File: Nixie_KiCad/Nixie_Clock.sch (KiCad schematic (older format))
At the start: 18 parts, among them U1 K155ID1, U10 K155ID1, U11 IN-14, U12 DS3231, U2 IN-14, U3 K155ID1, U4 IN-14, U5 K155ID1, U6 IN-3, U7 PS_V2H, U8 K155ID1, U9 IN-14

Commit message: Added PCB
-Added PCB ratsnest
-Added Netlist
-Changed Arduino module
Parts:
- removed A1: Arduino_UNO_R3, Module:Arduino_UNO_R3, symbol Nixie_Lib:Arduino_UNO_R3
- added A1: Arduino_Nano_Every, Module:Arduino_Nano, symbol Nixie_Lib:Arduino_Nano_Every
- added R4, R5, R6: 10k, Resistor_THT:R_Axial_DIN0207_L6.3mm_D2.5mm_P7.62mm_Horizontal, symbol Device:R
- added R7: 5k1, Resistor_THT:R_Axial_DIN0207_L6.3mm_D2.5mm_P7.62mm_Horizontal, symbol Device:R
- R1, R2: footprint (none) -> Resistor_THT:R_Axial_DIN0207_L6.3mm_D2.5mm_P7.62mm_Horizontal
- R3: value 137.5k -> 100k; footprint (none) -> Resistor_THT:R_Axial_DIN0207_L6.3mm_D2.5mm_P7.62mm_Horizontal
- R8: renamed from R4; footprint (none) -> Resistor_THT:R_Axial_DIN0207_L6.3mm_D2.5mm_P7.62mm_Horizontal
- R9: renamed from R5; footprint (none) -> Resistor_THT:R_Axial_DIN0207_L6.3mm_D2.5mm_P7.62mm_Horizontal
- U1, U10, U3, U5, U8: footprint (none) -> Nixie_Clock_Footprint:K155ID1
- U11, U2, U4, U9: footprint (none) -> Nixie_Clock_Footprint:IN-14
- U12: footprint (none) -> Nixie_Clock_Footprint:DS3231
- U6: footprint (none) -> Nixie_Clock_Footprint:IN-3
- U7: footprint (none) -> Nixie_Clock_Footprint:PS_V2H
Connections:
- wire segments 134 -> 146
- no-connect marks 29 -> 27
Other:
- note added: "Can add switch to cathode here to\npermanently turn on DEC"
- moved on the sheet: R3

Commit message: Finalized Design
- Finalized PCB design
- Generated Gerber files
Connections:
- net GND: no longer U12.6 (GND)
- net at A1.29 (GND), A1.4 (GND): now also U12.6 (GND)
- no-connect marks 27 -> 26
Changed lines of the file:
@@
 Wire Wire Line
 	6950 4500 6950 4400
-$Comp
-L power:GND #PWR021
-U 1 1 61CE0EAF
-P 6950 4700
-F 0 "#PWR021" H 6950 4450 50  0001 C CNN
-F 1 "GND" H 6955 4527 50  0000 C CNN
-F 2 "" H 6950 4700 50  0001 C CNN
-F 3 "" H 6950 4700 50  0001 C CNN
-	1    6950 4700
-	1    0    0    -1
-$EndComp
 Wire Wire Line
 	6950 4700 6950 4600
@@
 NoConn ~ 7650 2550
 $Comp
-L power:GND #PWR023
-U 1 1 61D94328
-P 1600 5450
-F 0 "#PWR023" H 1600 5200 50  0001 C CNN
-F 1 "GND" H 1605 5277 50  0000 C CNN
-F 2 "" H 1600 5450 50  0001 C CNN
-F 3 "" H 1600 5450 50  0001 C CNN
-	1    1600 5450
-	1    0    0    -1
-$EndComp
-$Comp
 L Nixie_Lib:IN-3 U6
 U 1 1 61DA4CEC
@@
 $EndComp
 Wire Wire Line
-	1600 5350 1600 5450
-Wire Wire Line
 	1600 4650 1500 4650
 $Comp
@@
 NoConn ~ 1200 3650
 NoConn ~ 1600 4050
-NoConn ~ 1700 2050
 $Comp
 L Nixie_Lib:Arduino_Nano_Every A1
@@
 	-1   0    0    1
 $EndComp
+Wire Wire Line
+	1600 5350 2550 5350
+Wire Wire Line
+	2550 5350 2550 2050
+Wire Wire Line
+	2550 2050 1700 2050
+$Comp
+L power:Earth #PWR?
+U 1 1 61D64376
+P 6950 4700
+F 0 "#PWR?" H 6950 4450 50  0001 C CNN
+F 1 "Earth" H 6950 4550 50  0001 C CNN
+F 2 "" H 6950 4700 50  0001 C CNN
+F 3 "~" H 6950 4700 50  0001 C CNN
+	1    6950 4700
+	1    0    0    -1
+$EndComp
 $EndSCHEMATC

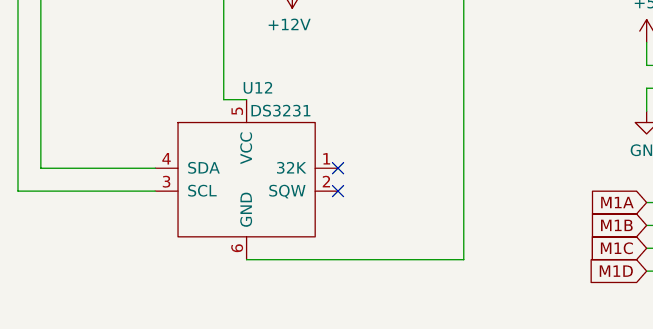
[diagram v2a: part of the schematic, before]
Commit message: Added Drill Holes
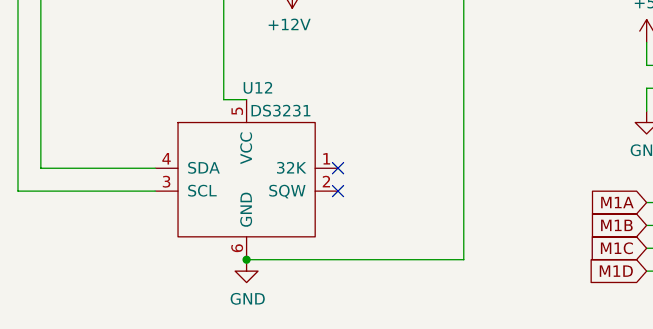
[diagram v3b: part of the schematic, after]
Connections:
- net GND: now also A1.29 (GND), A1.4 (GND), U12.6 (GND)
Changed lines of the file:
@@
 	1    0    0    -1
 $EndComp
+$Comp
+L power:GND #PWR?
+U 1 1 61CE4D4F
+P 1600 5350
+F 0 "#PWR?" H 1600 5100 50  0001 C CNN
+F 1 "GND" H 1605 5177 50  0000 C CNN
+F 2 "" H 1600 5350 50  0001 C CNN
+F 3 "" H 1600 5350 50  0001 C CNN
+	1    1600 5350
+	1    0    0    -1
+$EndComp
+Connection ~ 1600 5350
 $EndSCHEMATC

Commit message: minor updates
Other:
- note added: "Can add optional 100nF\nfilter capacitor here\nand/or voltage rectifier"
- note removed: "Can add optional 100nF\nfilter capacitor here"
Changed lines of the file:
@@
 $EndComp
 Text Notes 8400 4500 0    50   ~ 0
-Can add optional 100nF\nfilter capacitor here
+Can add optional 100nF\nfilter capacitor here\nand/or voltage rectifier
 $Comp
 L Nixie_Lib:DS3231 U12

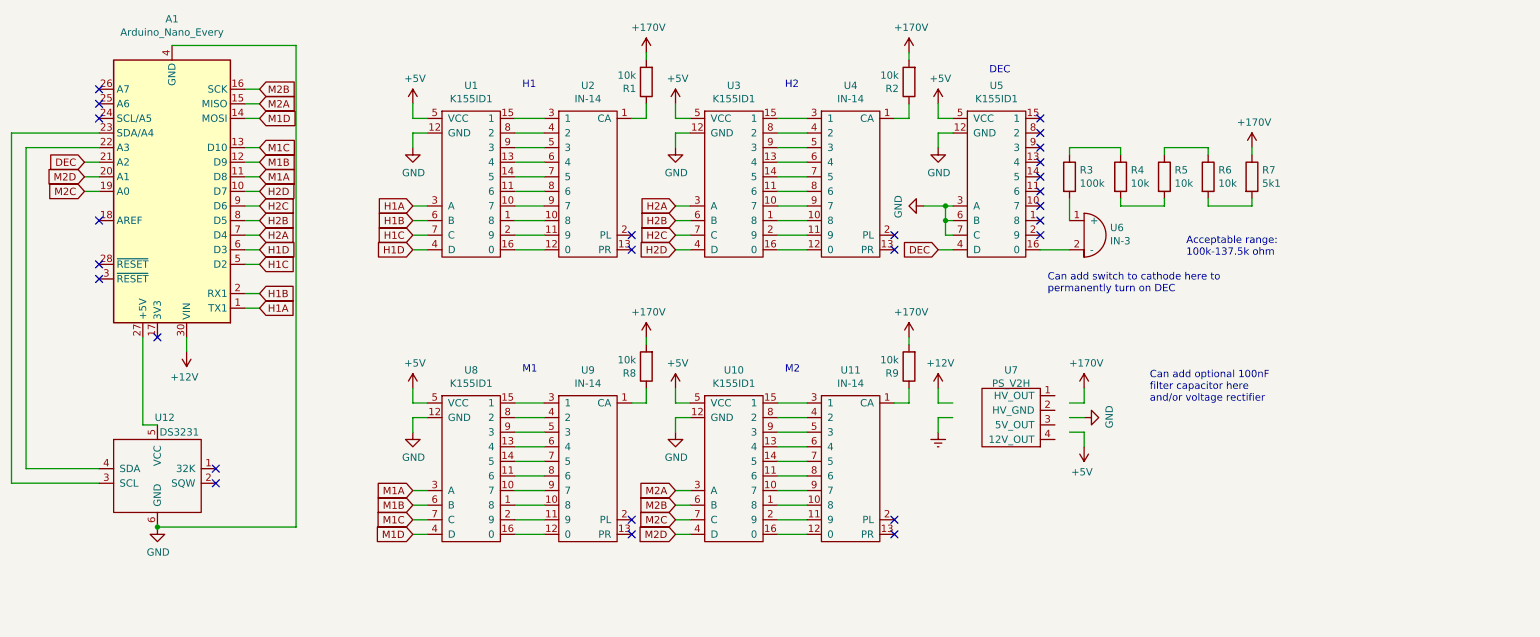
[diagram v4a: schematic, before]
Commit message: added filter capacitors
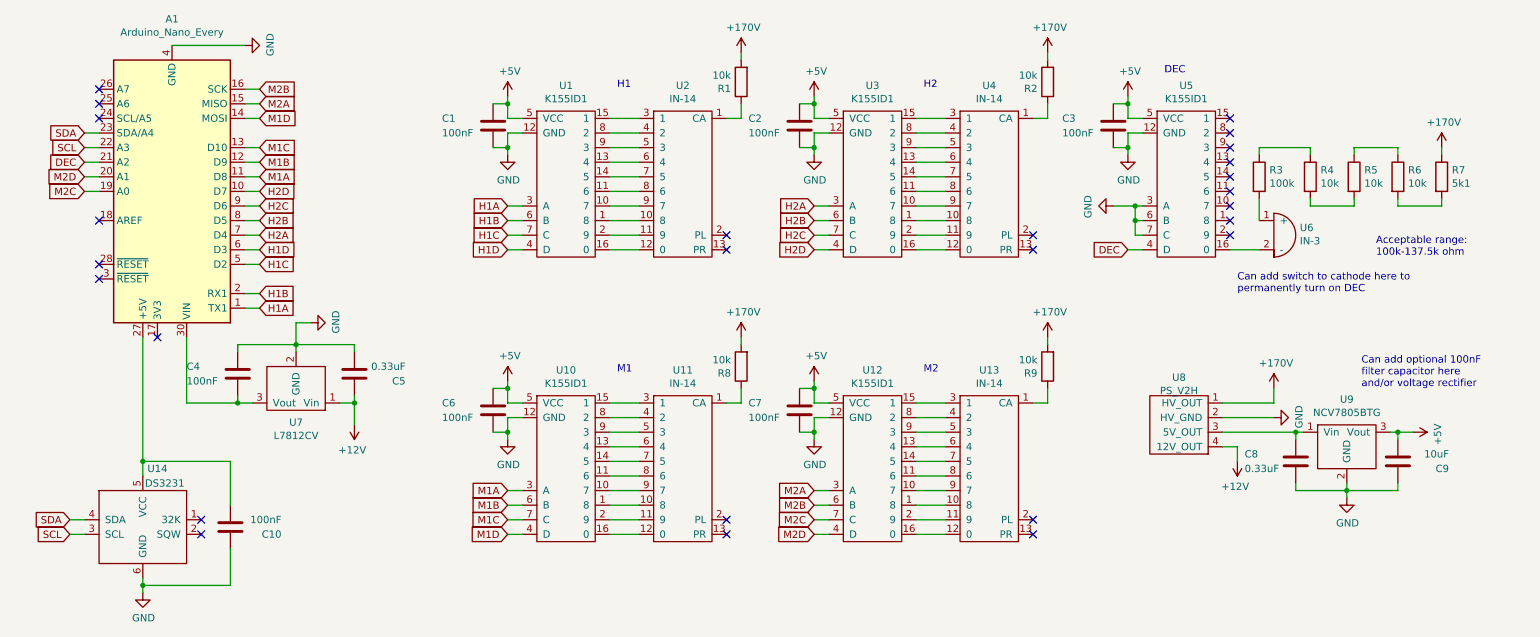
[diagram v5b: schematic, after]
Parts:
- added C1, C10, C2, C3, C4, C6, C7: 100nF, Capacitor_SMD:C_0402_1005Metric_Pad0.74x0.62mm_HandSolder, symbol Device:C
- added C5, C8: 0.33uF, Capacitor_SMD:C_1206_3216Metric_Pad1.33x1.80mm_HandSolder, symbol Device:C
- added C9: 10uF, Capacitor_SMD:C_0805_2012Metric_Pad1.18x1.45mm_HandSolder, symbol Device:C
- added U7: L7812CV, Nixie_Clock_Footprint:SIP-3, symbol Nixie_Lib:L7812CV
- added U9: NCV7805BTG, Nixie_Clock_Footprint:SIP-3, symbol Nixie_Lib:NCV7805BTG
- renumbered U8 to U10, U9 to U11, U10 to U12, U11 to U13, U12 to U14, U7 to U8
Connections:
- net +12V: now also U8.4 (12V_OUT), C5.2, U7.1 (Vin); no longer A1.30 (VIN)
- net +170V: now also U8.1 (HV_OUT)
- net +5V: now also C1.2, C2.2, C3.2, C6.2, C7.2, C9.1, U9.3 (Vout)
- net GND: now also U8.2 (HV_GND), C1.1, C10.2, C2.1, C3.1, C4.2, C5.1, C6.1, C7.1, C8.1, C9.2, U7.2 (GND), U9.2 (GND)
- net SCL: now reaches U14.3 (SCL)
- net SCL: now also A1.22 (A3); no longer A1.23 (SDA/A4)
- net SDA: now reaches U14.4 (SDA)
- net SDA: now also A1.23 (SDA/A4); no longer A1.22 (A3)
- net at A1.27 (+5V), U14.5 (VCC): now also C10.1
- net at U8.3 (5V_OUT): now also C8.2, U9.1 (Vin)
- new net: A1.30 (VIN), C4.1, U7.3 (Vout)
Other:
- moved on the sheet: R1, R2, R3, R4, R5, R6, R7, R8, R9, U1, U10, U11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

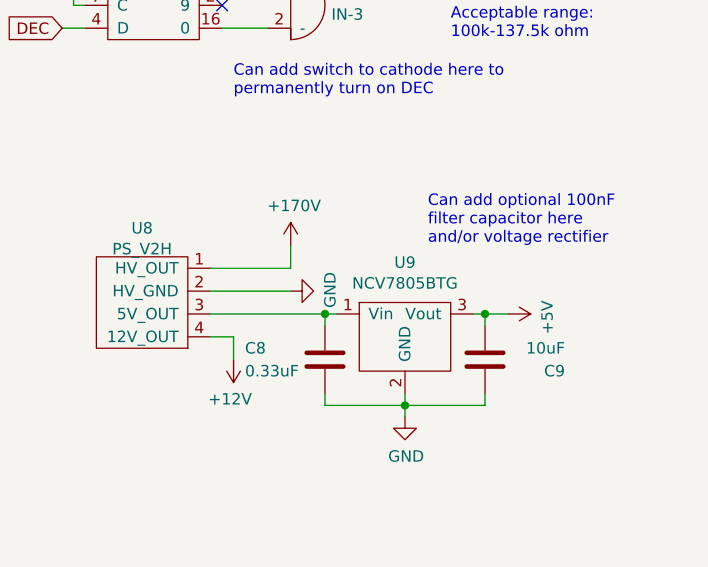
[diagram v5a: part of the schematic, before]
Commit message: updated footprints
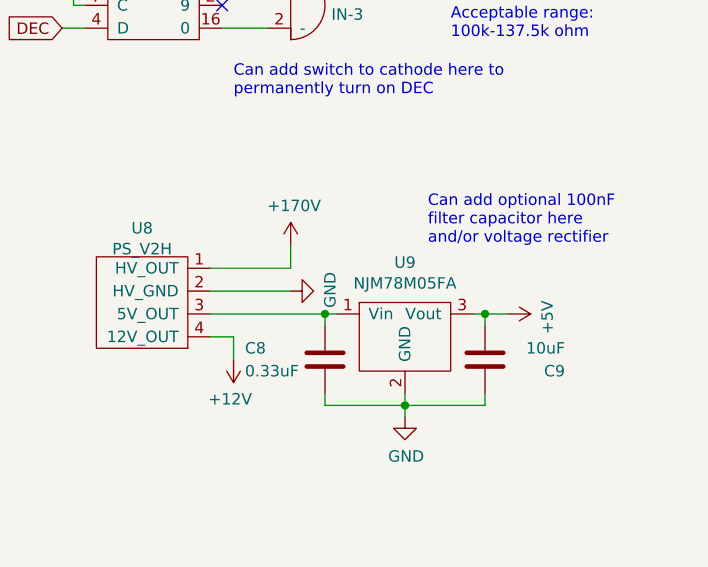
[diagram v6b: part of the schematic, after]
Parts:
- removed U9: NCV7805BTG, Nixie_Clock_Footprint:SIP-3, symbol Nixie_Lib:NCV7805BTG
- added U9: NJM78M05FA‎, Package_TO_SOT_THT:TO-220F-3_Horizontal_TabDown, symbol Nixie_Lib:NJM78M05FA‎
- U7: footprint Nixie_Clock_Footprint:SIP-3 -> Package_TO_SOT_THT:TO-220-3_Horizontal_TabDown
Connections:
- net +5V: now also U9.3 (Vout)
- net GND: now also U9.2 (GND)
- net at C8.2, U8.3 (5V_OUT): now also U9.1 (Vin)
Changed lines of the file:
@@
 Connection ~ 8250 2450
-$Comp
-L Nixie_Lib:NCV7805BTG U9
-U 1 1 61D73441
-P 9750 4850
-F 0 "U9" H 9750 5225 50  0000 C CNN
-F 1 "NCV7805BTG" H 9750 5134 50  0000 C CNN
-F 2 "Nixie_Clock_Footprint:SIP-3" H 9750 4850 50  0001 C CNN
-F 3 "" H 9750 4850 50  0001 C CNN
-	1    9750 4850
-	1    0    0    -1
-$EndComp
 $Comp
 L Nixie_Lib:L7812CV U7
@@
 F 0 "U7" H 2550 4633 50  0000 C CNN
 F 1 "L7812CV" H 2550 4724 50  0000 C CNN
-F 2 "Nixie_Clock_Footprint:SIP-3" H 2550 4350 50  0001 C CNN
+F 2 "Package_TO_SOT_THT:TO-220-3_Horizontal_TabDown" H 2550 4350 50  0001 C CNN
 F 3 "" H 2550 4350 50  0001 C CNN
 	1    2550 4350
@@
 	8900 4700 9400 4700
 $Comp
-L power:+12V #PWR?
+L power:+12V #PWR0101
 U 1 1 621063D4
 P 9000 4900
-F 0 "#PWR?" H 9000 4750 50  0001 C CNN
+F 0 "#PWR0101" H 9000 4750 50  0001 C CNN
 F 1 "+12V" H 9015 5073 50  0000 C CNN
 F 2 "" H 9000 4900 50  0001 C CNN
@@
 Wire Wire Line
 	9000 4800 9000 4900
+$Comp
+L Nixie_Lib:NJM78M05FA‎ U9
+U 1 1 61DA4461
+P 9750 4850
+F 0 "U9" H 9750 5225 50  0000 C CNN
+F 1 "NJM78M05FA‎" H 9750 5134 50  0000 C CNN
+F 2 "Package_TO_SOT_THT:TO-220F-3_Horizontal_TabDown" H 9750 4850 50  0001 C CNN
+F 3 "" H 9750 4850 50  0001 C CNN
+	1    9750 4850
+	1    0    0    -1
+$EndComp
 $EndSCHEMATC

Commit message: Uploaded Documentation
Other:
- note removed: "Can add optional 100nF\nfilter capacitor here\nand/or voltage rectifier"
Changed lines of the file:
@@
 Sheet 1 1
 Title "Nixie Clock"
-Date "2021-12-27"
+Date "2022-01-06"
 Rev "1.1"
 Comp "Michael Zheng"
@@
 	0    1    1    0
 $EndComp
-Text Notes 9850 4400 0    50   ~ 0
-Can add optional 100nF\nfilter capacitor here\nand/or voltage rectifier
 $Comp
 L Nixie_Lib:DS3231 U14

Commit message: Corrected RTC pinout
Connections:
- net SCL: now also A1.24 (SCL/A5); no longer A1.22 (A3)
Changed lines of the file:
@@
 Sheet 1 1
 Title "Nixie Clock"
-Date "2022-01-06"
-Rev "1.1"
+Date "2022-01-07"
+Rev "1.1.1"
 Comp "Michael Zheng"
 Comment1 ""
@@
 NoConn ~ 1200 2350
 NoConn ~ 1200 2450
-NoConn ~ 1200 2550
+NoConn ~ 1200 2750
 NoConn ~ 1200 3250
 NoConn ~ 1200 3550
@@
 Wire Wire Line
 	1100 5400 1000 5400
-Text GLabel 1100 2650 0    50   Input ~ 0
-SDA
-Text GLabel 1100 2750 0    50   Input ~ 0
+Text GLabel 1100 2550 0    50   Input ~ 0
 SCL
-Wire Wire Line
-	1100 2650 1200 2650
-Wire Wire Line
-	1200 2750 1100 2750
 Wire Wire Line
 	1500 4050 1500 4900
@@
 	1    0    0    -1
 $EndComp
+Wire Wire Line
+	1100 2650 1200 2650
+Text GLabel 1100 2650 0    50   Input ~ 0
+SDA
+Wire Wire Line
+	1100 2550 1200 2550
 $EndSCHEMATC
